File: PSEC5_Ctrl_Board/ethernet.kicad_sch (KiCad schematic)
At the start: 42 parts, among them Q6 NMOS, Q8 NMOS, T2 7499111446, U15 88E1512-A0-NNP2C000, Y3 ASE2-25.000MHZ-ET

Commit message: ERC "Done" (4 errors left) Schematic "Done"
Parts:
- removed U15: 88E1512-A0-NNP2C000, QFN_56P_MTG, symbol PSEC5_ctrlbd:88E1512-A0-NNP2C000
- added U1: 88E1512-A0-NNP2C000, QFN_56P_MTG, symbol PSEC5_ctrlbd:88E1512-A0-NNP2C000
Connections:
- net AVDD18: now also U1.19 (AVDD18), U1.26 (AVDD18), U1.3 (AVDD18), U1.35 (AVDDC18), U1.38 (AVDD18), U1.39 (AVDD18_OUT)
- net AVDD33: now also U1.20 (AVDD33), U1.25 (AVDD33)
- net DVDD: now also U1.40 (DVDD_OUT), U1.42 (DVDD), U1.6 (DVDD)
- net ETH_MDC: now also U1.7 (MDC)
- net ETH_MDIO: now also U1.8 (MDIO)
- net ETH_TXD0: now also U1.50 (TXD[0])
- net ETH_TXD1: now also U1.51 (TXD[1])
- net ETH_TXD2: now also U1.54 (TXD[2])
- net ETH_TXD3: now also U1.55 (TXD[3])
- net ETH_TX_CLK: now also U1.53 (TX_CLK)
- net ETH_TX_CTRL: now also U1.56 (TX_CTRL)
- net GND: now also U1.10 (VDDO_SEL), U1.11 (VDDO), U1.36 (REG_IN), U1.49 (VDDO), U1.52 (VDDO), U1.EPAD (VSS)
- net OSC25_OUT: now also U1.34 (XTAL_IN)
- net PHY_MDI0_N: now also U1.28 (MDIP[0])
- net PHY_MDI0_P: now also U1.27 (MDIN[0])
- net PHY_MDI1_N: now also U1.24 (MDIP[1])
- net PHY_MDI1_P: now also U1.23 (MDIN[1])
- net PHY_MDI2_N: now also U1.22 (MDIP[2])
- net PHY_MDI2_P: now also U1.21 (MDIN[2])
- net PHY_MDI3_N: now also U1.18 (MDIP[3])
- net PHY_MDI3_P: now also U1.17 (MDIN[3])
- net at R24.1: now also U1.47 (RXD[2])
- net at R28.1: now also U1.43 (RX_CTRL)
- net at R23.1: now also U1.48 (RXD[3])
- net at R78.1: now also U1.46 (RX_CLK)
- net at C155.1: now also U1.41 (REGCAP2)
- net at C155.2: now also U1.37 (REGCAP1)
- net at R26.1: now also U1.45 (RXD[1])
- net at R27.1: now also U1.44 (RXD[0])
- net at R84.2: now also U1.15 (CONFIG)
- net at R22.1: now also U1.30 (RSET)
- net 11 renamed LED_11
- net 13 renamed LED_13
- net LED_13: now also U1.13 (LED[1])
- net LED1_Y+ renamed LED_12
- net LED_12: now also U1.12 (LED[2]/INTn)
- net LED2_Y+ renamed LED_14
- net LED_14: now also U1.14 (LED[0])
- new net PS_POR: U1.16 (RESETn)
- no-connect marks 8 -> 9

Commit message: Changes
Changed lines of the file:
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@@
 	(wire
 		(pts
-			(xy 172.72 118.11) (xy 181.61 118.11)
+			(xy 172.72 118.11) (xy 186.69 118.11)
 		)
 		(stroke
@@
 	(wire
 		(pts
-			(xy 172.72 125.73) (xy 181.61 125.73)
+			(xy 172.72 125.73) (xy 190.5 125.73)
 		)
 		(stroke
@@
 	(wire
 		(pts
-			(xy 172.72 123.19) (xy 181.61 123.19)
+			(xy 172.72 123.19) (xy 190.5 123.19)
 		)
 		(stroke
@@
 	(wire
 		(pts
-			(xy 172.72 135.89) (xy 181.61 135.89)
+			(xy 172.72 135.89) (xy 190.5 135.89)
 		)
 		(stroke
@@
 	(wire
 		(pts
-			(xy 172.72 138.43) (xy 180.34 138.43)
+			(xy 172.72 138.43) (xy 190.5 138.43)
 		)
 		(stroke
@@
 	(wire
 		(pts
-			(xy 172.72 128.27) (xy 181.61 128.27)
+			(xy 172.72 128.27) (xy 190.5 128.27)
 		)
 		(stroke
@@
 	)
 	(label "DVDD_OUT"
-		(at 181.61 123.19 0)
-		(fields_autoplaced yes)
-		(effects
-			(font
-				(size 1.27 1.27)
-			)
-			(justify left bottom)
+		(at 190.5 123.19 180)
+		(fields_autoplaced yes)
+		(effects
+			(font
+				(size 1.27 1.27)
+			)
+			(justify right bottom)
 		)
 	)
@@
 	)
 	(label "DVDD"
-		(at 181.61 118.11 0)
-		(fields_autoplaced yes)
-		(effects
-			(font
-				(size 1.27 1.27)
-			)
-			(justify left bottom)
+		(at 186.69 118.11 180)
+		(fields_autoplaced yes)
+		(effects
+			(font
+				(size 1.27 1.27)
+			)
+			(justify right bottom)
 		)
 	)
@@
 	)
 	(label "AVDDC18"
-		(at 181.61 135.89 0)
-		(fields_autoplaced yes)
-		(effects
-			(font
-				(size 1.27 1.27)
-			)
-			(justify left bottom)
+		(at 190.5 135.89 180)
+		(fields_autoplaced yes)
+		(effects
+			(font
+				(size 1.27 1.27)
+			)
+			(justify right bottom)
 		)
 	)
@@
 	)
 	(label "AVDD18_OUT"
-		(at 181.61 125.73 0)
-		(fields_autoplaced yes)
-		(effects
-			(font
-				(size 1.27 1.27)
-			)
-			(justify left bottom)
+		(at 190.5 125.73 180)
+		(fields_autoplaced yes)
+		(effects
+			(font
+				(size 1.27 1.27)
+			)
+			(justify right bottom)
 		)
 	)
@@
 	)
 	(label "OSC25_OUT"
-		(at 180.34 138.43 0)
-		(fields_autoplaced yes)
-		(effects
-			(font
-				(size 1.27 1.27)
-			)
-			(justify left bottom)
+		(at 190.5 138.43 180)
+		(fields_autoplaced yes)
+		(effects
+			(font
+				(size 1.27 1.27)
+			)
+			(justify right bottom)
 		)
 	)
@@
 	)
 	(label "AVDD18"
-		(at 181.61 128.27 0)
-		(fields_autoplaced yes)
-		(effects
-			(font
-				(size 1.27 1.27)
-			)
-			(justify left bottom)
-		)
-	)
+		(at 190.5 128.27 180)
+		(fields_autoplaced yes)
+		(effects
+			(font
+				(size 1.27 1.27)
+			)
+			(justify right bottom)
+		)
+	)

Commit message: My PC is fading, pushing in case it dies
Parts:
- 1M2, L3, L5, R22, R23, R24, R26, R27, R28, R78, R84: footprint (none) -> Resistor_SMD:R_0603_1608Metric
- Q6, Q8: footprint (none) -> SI2342DS_T1_GE3:SOT-23_TO-236_VIS
- T2: footprint WE-RJ45_7499111446:7499111446 -> Connector_RJ:RJ45_Wuerth_7499111446_Horizontal
- U1: footprint QFN_56P_MTG -> 88E1512_A0_NNP2C000:QFN_56P_MTG
- Y3: footprint ASE2-25.000MHZ-ET:XTAL_ASE2-25.000MHZ-ET -> ASE2_25_000MHZ_ET:XTAL_ASE2-25.000MHZ-ET
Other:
- note added: "742863122"
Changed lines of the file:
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@@
 		)
 	)
+	(text "742863122"
+		(exclude_from_sim no)
+		(at 37.846 219.202 0)
+		(effects
+			(font
+				(size 1.27 1.27)
+			)
+		)
+	)
 	(text "ETHERNET\n"
 		(exclude_from_sim no)
@@
 		)
 	)
+	(text "742863122"
+		(exclude_from_sim no)
+		(at 55.88 125.222 0)
+		(effects
+			(font
+				(size 1.27 1.27)
+			)
+		)
+	)
 	(label "LED_12"
 		(at 96.52 107.95 0)
@@
 			)
 		)
-		(property "Footprint" "WE-RJ45_7499111446:7499111446"
+		(property "Footprint" "Connector_RJ:RJ45_Wuerth_7499111446_Horizontal"
 			(at 136.144 8.636 0)
 			(effects
@@
 			)
 		)
-		(property "Footprint" ""
+		(property "Footprint" "Resistor_SMD:R_0603_1608Metric"
 			(at 189.484 104.394 90)
 			(effects
@@
 			)
 		)
-		(property "Footprint" ""
+		(property "Footprint" "Resistor_SMD:R_0603_1608Metric"
 			(at 189.484 114.554 90)
 			(effects
@@
 			)
 		)
-		(property "Footprint" ""
+		(property "Footprint" "Resistor_SMD:R_0603_1608Metric"
 			(at 189.484 101.854 90)
 			(effects
@@
 			)
 		)
-		(property "Footprint" "ASE2-25.000MHZ-ET:XTAL_ASE2-25.000MHZ-ET"
+		(property "Footprint" "ASE2_25_000MHZ_ET:XTAL_ASE2-25.000MHZ-ET"
 			(at 256.54 119.888 0)
 			(effects
@@
 			)
 		)
-		(property "Footprint" ""
+		(property "Footprint" "Resistor_SMD:R_0603_1608Metric"
 			(at 189.484 106.934 90)
 			(effects
@@
 			)
 		)
-		(property "Footprint" ""
+		(property "Footprint" "SI2342DS_T1_GE3:SOT-23_TO-236_VIS"
 			(at 228.6 41.91 0)
 			(effects
@@
 			)
 		)
-		(property "Footprint" ""
+		(property "Footprint" "SI2342DS_T1_GE3:SOT-23_TO-236_VIS"
 			(at 228.6 21.59 0)
 			(effects
@@
 			)
 		)
-		(property "Footprint" ""
+		(property "Footprint" "Resistor_SMD:R_0603_1608Metric"
 			(at 38.1 223.52 0)
 			(effects
@@
 			)
 		)
-		(property "Footprint" ""
+		(property "Footprint" "Resistor_SMD:R_0603_1608Metric"
 			(at 138.684 62.484 90)
 			(effects
@@
 			)
 		)
-		(property "Footprint" ""
+		(property "Footprint" "Resistor_SMD:R_0603_1608Metric"
 			(at 189.484 109.474 90)
 			(effects
@@
 			)
 		)
-		(property "Footprint" ""
+		(property "Footprint" "Resistor_SMD:R_0603_1608Metric"
 			(at 189.484 112.014 90)
 			(effects
@@
 			)
 		)
-		(property "Footprint" ""
+		(property "Footprint" "Resistor_SMD:R_0603_1608Metric"
 			(at 92.964 114.554 90)
 			(effects
@@
 			)
 		)
-		(property "Footprint" ""
+		(property "Footprint" "Resistor_SMD:R_0603_1608Metric"
 			(at 57.15 128.27 0)
 			(effects
@@
 			)
 		)
-		(property "Footprint" "QFN_56P_MTG"
+		(property "Footprint" "88E1512_A0_NNP2C000:QFN_56P_MTG"
 			(at 122.682 64.262 0)
 			(effects
@@
 			)
 		)
-		(property "Footprint" ""
+		(property "Footprint" "Resistor_SMD:R_0603_1608Metric"
 			(at 183.134 147.574 90)
 			(effects

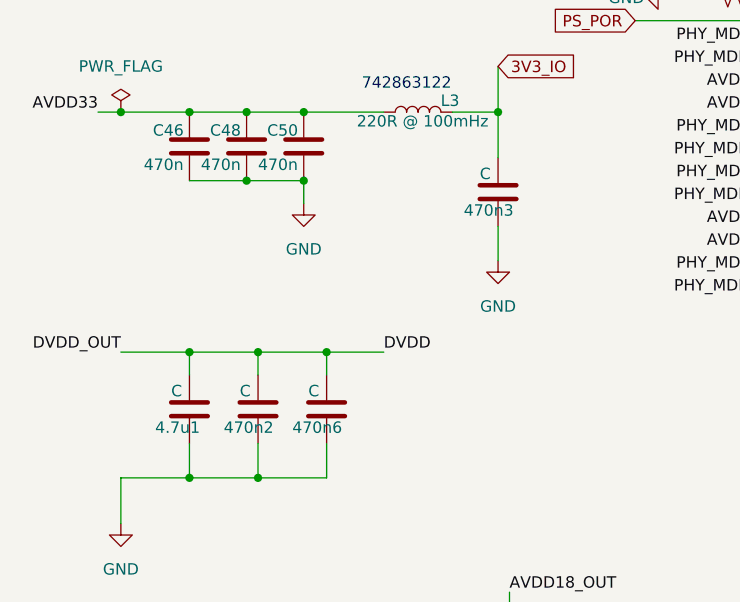
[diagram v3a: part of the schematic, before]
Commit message: rearranged samtec
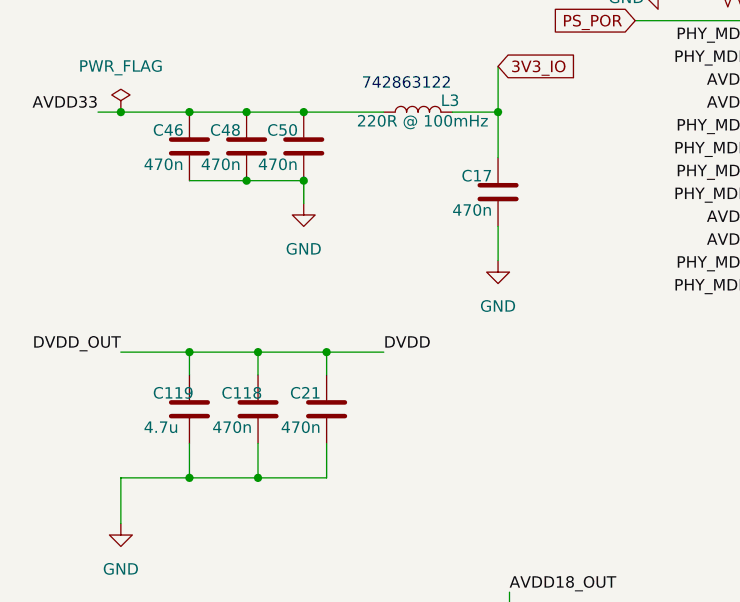
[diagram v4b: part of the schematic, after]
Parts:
- removed 4.7u1, 470n2, 470n3, 470n6: C, Capacitor_SMD:C_0603_1608Metric, symbol Device:C
- added C118, C17, C21: 470n, Capacitor_SMD:C_0603_1608Metric, symbol Device:C
- added C119: 4.7u, Capacitor_SMD:C_0603_1608Metric, symbol Device:C
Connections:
- net DVDD: now also C118.1, C119.1, C21.1
- net GND: now also C118.2, C119.2, C17.1, C17.2, C21.2
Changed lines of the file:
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@@
 	(symbol
 		(lib_id "Device:C")
+		(at 66.04 137.16 0)
+		(unit 1)
+		(exclude_from_sim no)
+		(in_bom yes)
+		(on_board yes)
+		(dnp no)
+		(property "Reference" "C17"
+			(at 61.976 135.382 0)
+			(effects
+				(font
+					(size 1.27 1.27)
+				)
+				(justify left)
+			)
+		)
+		(property "Value" "470n"
+			(at 60.96 139.192 0)
+			(effects
+				(font
+					(size 1.27 1.27)
+				)
+				(justify left)
+			)
+		)
+		(property "Footprint" "Capacitor_SMD:C_0603_1608Metric"
+			(at 67.0052 140.97 0)
+			(effects
+				(font
+					(size 1.27 1.27)
+				)
+				(hide yes)
+			)
+		)
+		(property "Datasheet" "~"
+			(at 66.04 137.16 0)
+			(effects
+				(font
+					(size 1.27 1.27)
+				)
+				(hide yes)
+			)
+		)
+		(property "Description" "Unpolarized capacitor"
+			(at 66.04 137.16 0)
+			(effects
+				(font
+					(size 1.27 1.27)
+				)
+				(hide yes)
+			)
+		)
+		(pin "1"
+		)
+		(pin "2"
+		)
+		(instances
+			(project "PSEC5_Ctrl_Board"
+				(path "/165f2ae6-d522-4adf-a6c4-bb137b209d33/1f6d7a03-cfad-4370-8d2b-49ab19e248d8/6e9ff0d5-3c45-486c-9945-94fa6223df4a"
+					(reference "C17")
+					(unit 1)
+				)
+			)
+		)
+	)
+	(symbol
+		(lib_id "Device:C")
 		(at 43.18 189.23 0)
 		(unit 1)
@@
 	)
 	(symbol
-		(lib_id "Device:C")
-		(at 39.37 161.29 0)
-		(unit 1)
-		(exclude_from_sim no)
-		(in_bom yes)
-		(on_board yes)
-		(dnp no)
-		(property "Reference" "470n2"
-			(at 35.56 163.322 0)
-			(effects
-				(font
-					(size 1.27 1.27)
-				)
-				(justify left)
-			)
-		)
-		(property "Value" "C"
-			(at 37.338 159.258 0)
-			(effects
-				(font
-					(size 1.27 1.27)
-				)
-				(justify left)
-			)
-		)
-		(property "Footprint" "Capacitor_SMD:C_0603_1608Metric"
-			(at 40.3352 165.1 0)
-			(effects
-				(font
-					(size 1.27 1.27)
-				)
-				(hide yes)
-			)
-		)
-		(property "Datasheet" "~"
-			(at 39.37 161.29 0)
-			(effects
-				(font
-					(size 1.27 1.27)
-				)
-				(hide yes)
-			)
-		)
-		(property "Description" "Unpolarized capacitor"
-			(at 39.37 161.29 0)
-			(effects
-				(font
-					(size 1.27 1.27)
-				)
-				(hide yes)
-			)
-		)
-		(pin "2"
-		)
-		(pin "1"
-		)
-		(instances
-			(project "PSEC5_Ctrl_Board"
-				(path "/165f2ae6-d522-4adf-a6c4-bb137b209d33/1f6d7a03-cfad-4370-8d2b-49ab19e248d8/6e9ff0d5-3c45-486c-9945-94fa6223df4a"
-					(reference "470n2")
-					(unit 1)
-				)
-			)
-		)
-	)
-	(symbol
 		(lib_id "PSEC5_ctrlbd:ASE2-25.000MHZ-ET")
 		(at 270.51 138.43 0)
@@
 	)
 	(symbol
-		(lib_id "Device:R_Small_US")
-		(at 245.11 19.05 90)
+		(lib_id "Device:C")
+		(at 39.37 161.29 0)
 		(unit 1)
 		(exclude_from_sim no)
@@
 		(on_board yes)
 		(dnp no)
-		(property "Reference" "R74"
-			(at 241.808 18.034 90)
+		(property "Reference" "C118"
+			(at 35.306 159.512 0)
 			(effects
 				(font
 					(size 1.27 1.27)
 				)
+				(justify left)
 			)
 		)
-		(property "Value" "240R"
-			(at 249.174 18.034 90)
+		(property "Value" "470n"
+			(at 34.29 163.322 0)
 			(effects
 				(font
 					(size 1.27 1.27)
 				)
+				(justify left)
 			)
 		)
-		(property "Footprint" "Resistor_SMD:R_0603_1608Metric"
-			(at 245.11 19.05 0)
+		(property "Footprint" "Capacitor_SMD:C_0603_1608Metric"
+			(at 40.3352 165.1 0)
 			(effects
 				(font
@@
 		)
 		(property "Datasheet" "~"
-			(at 245.11 19.05 0)
+			(at 39.37 161.29 0)
 			(effects
 				(font
@@
 			)
 		)
-		(property "Description" "Resistor, small US symbol"
-			(at 245.11 19.05 0)
+		(property "Description" "Unpolarized capacitor"
+			(at 39.37 161.29 0)
 			(effects
 				(font
@@
 			(project "PSEC5_Ctrl_Board"
 				(path "/165f2ae6-d522-4adf-a6c4-bb137b209d33/1f6d7a03-cfad-4370-8d2b-49ab19e248d8/6e9ff0d5-3c45-486c-9945-94fa6223df4a"
-					(reference "R74")
+					(reference "C118")
 					(unit 1)
 				)
@@
 	)
 	(symbol
-		(lib_id "Device:C")
-		(at 66.04 137.16 0)
+		(lib_id "Device:R_Small_US")
+		(at 245.11 19.05 90)
 		(unit 1)
 		(exclude_from_sim no)
@@
 		(on_board yes)
 		(dnp no)
-		(property "Reference" "470n3"
-			(at 62.23 139.192 0)
+		(property "Reference" "R74"
+			(at 241.808 18.034 90)
 			(effects
 				(font
 					(size 1.27 1.27)
 				)
-				(justify left)
 			)
 		)
-		(property "Value" "C"
-			(at 64.008 135.128 0)
+		(property "Value" "240R"
+			(at 249.174 18.034 90)
 			(effects
 				(font
 					(size 1.27 1.27)
 				)
-				(justify left)
 			)
 		)
-		(property "Footprint" "Capacitor_SMD:C_0603_1608Metric"
-			(at 67.0052 140.97 0)
+		(property "Footprint" "Resistor_SMD:R_0603_1608Metric"
+			(at 245.11 19.05 0)
 			(effects
 				(font
@@
 		)
 		(property "Datasheet" "~"
-			(at 66.04 137.16 0)
+			(at 245.11 19.05 0)
 			(effects
 				(font
@@
 			)
 		)
-		(property "Description" "Unpolarized capacitor"
-			(at 66.04 137.16 0)
+		(property "Description" "Resistor, small US symbol"
+			(at 245.11 19.05 0)
 			(effects
 				(font
@@
 			)
 		)
-		(pin "2"
-		)
 		(pin "1"
 		)
+		(pin "2"
+		)
 		(instances
 			(project "PSEC5_Ctrl_Board"
 				(path "/165f2ae6-d522-4adf-a6c4-bb137b209d33/1f6d7a03-cfad-4370-8d2b-49ab19e248d8/6e9ff0d5-3c45-486c-9945-94fa6223df4a"
-					(reference "470n3")
+					(reference "R74")
 					(unit 1)
 				)
@@
 	)
 	(symbol
+		(lib_id "Device:C")
+		(at 31.75 161.29 0)
+		(unit 1)
+		(exclude_from_sim no)
+		(in_bom yes)
+		(on_board yes)
+		(dnp no)
+		(property "Reference" "C119"
+			(at 27.686 159.512 0)
+			(effects
+				(font
+					(size 1.27 1.27)
+				)
+				(justify left)
+			)
+		)
+		(property "Value" "4.7u"
+			(at 26.67 163.322 0)
+			(effects
+				(font
+					(size 1.27 1.27)
+				)
+				(justify left)
+			)
+		)
+		(property "Footprint" "Capacitor_SMD:C_0603_1608Metric"
+			(at 32.7152 165.1 0)
+			(effects
+				(font
+					(size 1.27 1.27)
+				)
+				(hide yes)
+			)
+		)
+		(property "Datasheet" "~"
+			(at 31.75 161.29 0)
+			(effects
+				(font
+					(size 1.27 1.27)
+				)
+				(hide yes)
+			)
+		)
+		(property "Description" "Unpolarized capacitor"
+			(at 31.75 161.29 0)
+			(effects
+				(font
+					(size 1.27 1.27)
+				)
+				(hide yes)
+			)
+		)
+		(pin "1"
+		)
+		(pin "2"
+		)
+		(instances
+			(project "PSEC5_Ctrl_Board"
+				(path "/165f2ae6-d522-4adf-a6c4-bb137b209d33/1f6d7a03-cfad-4370-8d2b-49ab19e248d8/6e9ff0d5-3c45-486c-9945-94fa6223df4a"
+					(reference "C119")
+					(unit 1)
+				)
+			)
+		)
+	)
+	(symbol
 		(lib_id "Device:R_US")
 		(at 189.23 110.49 90)
@@
 		(on_board yes)
 		(dnp no)
-		(property "Reference" "470n6"
-			(at 43.18 163.322 0)
+		(property "Reference" "C21"
+			(at 42.926 159.512 0)
 			(effects
 				(font
@@
 			)
 		)
-		(property "Value" "C"
-			(at 44.958 159.258 0)
+		(property "Value" "470n"
+			(at 41.91 163.322 0)
 			(effects
 				(font
@@
 			)
 		)
-		(pin "2"
-		)
 		(pin "1"
 		)
+		(pin "2"
+		)
 		(instances
 			(project "PSEC5_Ctrl_Board"
 				(path "/165f2ae6-d522-4adf-a6c4-bb137b209d33/1f6d7a03-cfad-4370-8d2b-49ab19e248d8/6e9ff0d5-3c45-486c-9945-94fa6223df4a"
-					(reference "470n6")
+					(reference "C21")
 					(unit 1)
 				)
@@
 					(unit 1)
 				)
-			)
-		)
-	)
-	(symbol
-		(lib_id "Device:C")
-		(at 31.75 161.29 0)
-		(unit 1)
-		(exclude_from_sim no)
-		(in_bom yes)
-		(on_board yes)
-		(dnp no)
-		(property "Reference" "4.7u1"
-			(at 27.94 163.322 0)
-			(effects
-				(font
-					(size 1.27 1.27)
-				)
-				(justify left)
-			)
-		)
-		(property "Value" "C"
-			(at 29.718 159.258 0)
-			(effects
-				(font
-					(size 1.27 1.27)
-				)
-				(justify left)
-			)
-		)
-		(property "Footprint" "Capacitor_SMD:C_0603_1608Metric"
-			(at 32.7152 165.1 0)
-			(effects
-				(font
-					(size 1.27 1.27)
-				)
-				(hide yes)
-			)
-		)
-		(property "Datasheet" "~"
-			(at 31.75 161.29 0)
-			(effects
-				(font
-					(size 1.27 1.27)
-				)
-				(hide yes)
-			)
-		)
-		(property "Description" "Unpolarized capacitor"
-			(at 31.75 161.29 0)
-			(effects
-				(font
-					(size 1.27 1.27)
-				)
-				(hide yes)
-			)
-		)
-		(pin "2"
-		)
-		(pin "1"
-		)
-		(instances
-			(project "PSEC5_Ctrl_Board"
-				(path "/165f2ae6-d522-4adf-a6c4-bb137b209d33/1f6d7a03-cfad-4370-8d2b-49ab19e248d8/6e9ff0d5-3c45-486c-9945-94fa6223df4a"
-					(reference "4.7u1")
-					(unit 1)
-				)

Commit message: Small Additions
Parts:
- removed T2: 7499111446, Connector_RJ:RJ45_Wuerth_7499111446_Horizontal, symbol PSEC5_ctrlbd:WE-RJ45_7499111446
- added T1: 7499111446, Connector_RJ:RJ45_Wuerth_7499111446_Horizontal, symbol PSEC5_ctrlbd:WE-RJ45_7499111446
- U1: footprint 88E1512_A0_NNP2C000:QFN_56P_MTG -> QFN_56P_MTG
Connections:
- net GND: now also U1.57 (VSS), T1.10 (GND); no longer C17.1, C58.1, C59.1, C61.1, C62.1, C63.1, C64.1, L3.2, L5.2, R74.2, R76.2, U1.10 (VDDO_SEL), U1.11 (VDDO), U1.36 (REG_IN), U1.49 (VDDO), U1.52 (VDDO), U1.EPAD (VSS)
- net LED_11: now also T1.11
- net LED_12: now also T1.12
- net LED_13: now also T1.13
- net LED_14: now also T1.14
- net PHY_MDI0_N: now also T1.3 (D1-)
- net PHY_MDI0_P: now also T1.2 (D1+)
- net PHY_MDI1_N: now also T1.5 (D2-)
- net PHY_MDI1_P: now also T1.4 (D2+)
- net PHY_MDI2_N: now also T1.7 (D3-)
- net PHY_MDI2_P: now also T1.6 (D3+)
- net PHY_MDI3_N: now also T1.9 (D4-)
- net PHY_MDI3_P: now also T1.8 (D4+)
- net PHY_VCC: now also T1.1 (VCC)
- net at 1M2.1, C57.1: now also T1.S1 (SHIELD1), T1.S2 (SHIELD2)
- new net 3V3_IO: C17.1, C58.1, C59.1, C61.1, C62.1, C63.1, C64.1, L3.2, L5.2, R74.2, R76.2, U1.10 (VDDO_SEL), U1.11 (VDDO), U1.36 (REG_IN), U1.49 (VDDO), U1.52 (VDDO)

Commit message: changes
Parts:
- removed 1M2: R_US, Resistor_SMD:R_0603_1608Metric, symbol Device:R_US
- added R100: 1M2, Resistor_SMD:R_0603_1608Metric, symbol Device:R_US
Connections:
- net GND: now also R100.2
- net at C57.1, T1.S1 (SHIELD1), T1.S2 (SHIELD2): now also R100.1
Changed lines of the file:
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@@
+	)
+	(symbol
+		(lib_id "Device:R_US")
+		(at 138.43 63.5 90)
+		(unit 1)
+		(exclude_from_sim no)
+		(in_bom yes)
+		(on_board yes)
+		(dnp no)
+		(property "Reference" "R100"
+			(at 141.986 62.484 90)
+			(effects
+				(font
+					(size 1.27 1.27)
+				)
+			)
+		)
+		(property "Value" "1M2"
+			(at 134.366 62.484 90)
+			(effects
+				(font
+					(size 1.27 1.27)
+				)
+			)
+		)
+		(property "Footprint" "Resistor_SMD:R_0603_1608Metric"
+			(at 138.684 62.484 90)
+			(effects
+				(font
+					(size 1.27 1.27)
+				)
+				(hide yes)
+			)
+		)
+		(property "Datasheet" "~"
+			(at 138.43 63.5 0)
+			(effects
+				(font
+					(size 1.27 1.27)
+				)
+				(hide yes)
+			)
+		)
+		(property "Description" "Resistor, US symbol"
+			(at 138.43 63.5 0)
+			(effects
+				(font
+					(size 1.27 1.27)
+				)
+				(hide yes)
+			)
+		)
+		(pin "1"
+		)
+		(pin "2"
+		)
+		(instances
+			(project "PSEC5_Ctrl_Board"
+				(path "/165f2ae6-d522-4adf-a6c4-bb137b209d33/1f6d7a03-cfad-4370-8d2b-49ab19e248d8/6e9ff0d5-3c45-486c-9945-94fa6223df4a"
+					(reference "R100")
+					(unit 1)
+				)
+			)
+		)
 	)
 	(symbol
@@
 					(unit 1)
 				)
-			)
-		)
-	)
-	(symbol
-		(lib_id "Device:R_US")
-		(at 138.43 63.5 90)
-		(unit 1)
-		(exclude_from_sim no)
-		(in_bom yes)
-		(on_board yes)
-		(dnp no)
-		(property "Reference" "1M2"
-			(at 142.24 64.77 90)
-			(effects
-				(font
-					(size 1.27 1.27)
-				)
-			)
-		)
-		(property "Value" "R_US"
-			(at 134.62 65.278 90)
-			(effects
-				(font
-					(size 1.27 1.27)
-				)
-			)
-		)
-		(property "Footprint" "Resistor_SMD:R_0603_1608Metric"
-			(at 138.684 62.484 90)
-			(effects
-				(font
-					(size 1.27 1.27)
-				)
-				(hide yes)
-			)
-		)
-		(property "Datasheet" "~"
-			(at 138.43 63.5 0)
-			(effects
-				(font
-					(size 1.27 1.27)
-				)
-				(hide yes)
-			)
-		)
-		(property "Description" "Resistor, US symbol"
-			(at 138.43 63.5 0)
-			(effects
-				(font
-					(size 1.27 1.27)
-				)
-				(hide yes)
-			)
-		)
-		(pin "2"
-		)
-		(pin "1"
-		)
-		(instances
-			(project "PSEC5_Ctrl_Board"
-				(path "/165f2ae6-d522-4adf-a6c4-bb137b209d33/1f6d7a03-cfad-4370-8d2b-49ab19e248d8/6e9ff0d5-3c45-486c-9945-94fa6223df4a"
-					(reference "1M2")
-					(unit 1)
-				)
